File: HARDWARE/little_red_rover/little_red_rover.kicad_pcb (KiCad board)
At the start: 2 copper layers, 127.3 x 82.2 mm, 38 parts, among them J1 USB_C_Receptacle_USB2.0_14P, J2 Conn_01x04_Socket, J3 Conn_01x02_Socket, J4 Conn_01x02_Socket, U1 ESP32-C3-MINI-1, U2 BQ24230RGT, U3 MIC5504-3.3YM5, U4 MIC2876-5.0YMT-TR, U5 DRV8212P, U6 DRV8212P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

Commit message: v1.0 board layout
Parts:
- added R14: 10k, Capacitor_SMD:C_0603_1608Metric_Pad1.08x0.95mm_HandSolder, F.Cu at (190.0, 104.4)
- added R15: 10k, Capacitor_SMD:C_0603_1608Metric_Pad1.08x0.95mm_HandSolder, F.Cu at (190.0, 106.0)
- added U9: LSM6DS3, Package_LGA:LGA-14_3x2.5mm_P0.5mm_LayoutBorder3x4y, F.Cu at (190.0, 110.0)
- J1: footprint Connector_USB:USB_C_Receptacle_GCT_USB4135-GF-A_6P_TopMnt_Horizontal -> Connector_USB:USB_C_Receptacle_GCT_USB4105-xx-A_16P_TopMnt_Horizontal
- moved R12 131.9 mm to (195.5, 112.5)
- moved R10 130.7 mm to (203.6, 92.0), turned to 180 degrees
- moved R5 121.8 mm to (154.9, 134.8), turned to 180 degrees
- moved R4 121.6 mm to (150.9, 134.8)
- moved R11 120.4 mm to (194.1, 90.5)
- moved R2 119.9 mm to (144.7, 131.6)
- moved R9 107.5 mm to (119.4, 131.2), turned to -90 degrees
- moved R1 107.5 mm to (140.8, 131.7), turned to 180 degrees
- moved C6 102.0 mm to (119.4, 134.7), turned to -90 degrees
- moved C4 97.9 mm to (117.4, 126.1)
- moved R3 95.7 mm to (108.5, 123.3), turned to 90 degrees
- moved C3 94.3 mm to (116.4, 120.1), turned to 180 degrees
- moved C1 94.0 mm to (106.5, 118.3), turned to 90 degrees
- moved C5 90.5 mm to (110.5, 123.3), turned to -90 degrees
- moved C2 89.1 mm to (110.5, 114.3), turned to 90 degrees
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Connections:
- C1 pad 1: +5V -> /usb_5v
- J1 pad A9: +5V -> /usb_5v
- J1 pad B9: +5V -> /usb_5v
- U1 pad 5: unconnected-(U1-GPIO2/ADC1_CH2-Pad5) -> /imu_scl
- U1 pad 6: unconnected-(U1-GPIO3/ADC1_CH3-Pad6) -> /imu_sda
- U2 pad 13: +5V -> /usb_5v
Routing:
- net +3.3V: track 0.00 -> 251.1 mm, vias 0 -> 2
- net +5V: track 0.00 -> 217.3 mm, vias 0 -> 5
- net /motor_sleep: track 0.00 -> 106.0 mm, vias 0 -> 3
- net /lidar_tx: track 0.00 -> 98.8 mm, vias 0 -> 2
- net /charger_out: track 0.00 -> 91.8 mm, vias 0 -> 2
- net Net-(D2-K): track 0.00 -> 89.3 mm
- net /usb_data_+: track 0.00 -> 81.9 mm, vias 0 -> 2
- net Net-(D1-K): track 0.00 -> 80.1 mm
- net /usb_data_-: track 0.00 -> 77.5 mm, vias 0 -> 2
- net /usb_5v: track 0.00 -> 72.5 mm
- net /left_motor_pwm_b: track 0.00 -> 55.9 mm, vias 0 -> 2
- net /left_motor_pwm_a: track 0.00 -> 54.6 mm, vias 0 -> 2
- net /right_motor_pwm_b: track 0.00 -> 52.2 mm, vias 0 -> 2
- net Net-(BT1-+): track 0.00 -> 52.1 mm, vias 0 -> 3
- net /right_motor_pwm_a: track 0.00 -> 46.9 mm
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- added copper zone on B.Cu, net GND
- added copper zone on F.Cu, net GND
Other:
- board text added: "little red rover v1.0"

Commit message: Update pcb outline, add threaded inserts
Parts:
- added C10: 0.1uF, Capacitor_SMD:C_0603_1608Metric_Pad1.08x0.95mm_HandSolder, F.Cu at (162.0, 86.8)
- added C7: 10uF, Capacitor_SMD:C_0603_1608Metric_Pad1.08x0.95mm_HandSolder, F.Cu at (156.2, 110.0)
- added C8: 10uF, Capacitor_SMD:C_0603_1608Metric_Pad1.08x0.95mm_HandSolder, F.Cu at (159.6, 85.8)
- added C9: 0.1uF, Capacitor_SMD:C_0603_1608Metric_Pad1.08x0.95mm_HandSolder, F.Cu at (159.4, 113.0)
- added REF**: m3_threaded_insert, digikey_imports:m3_threaded_insert, F.Cu at (163.5, 81.9)
- added REF**: m3_threaded_insert, digikey_imports:m3_threaded_insert, F.Cu at (163.5, 117.9)
- added REF**: m3_threaded_insert, digikey_imports:m3_threaded_insert, F.Cu at (92.2, 99.9)
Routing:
- net +3.3V: track 251.1 -> 260.8 mm, vias 2 -> 4
- net /left_motor_pwm_b: track 55.9 -> 55.0 mm
- net +5V: track 217.3 -> 217.6 mm, vias 5 -> 7
- net GND: vias 23 -> 28
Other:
- outline, holes or cut-outs redrawn

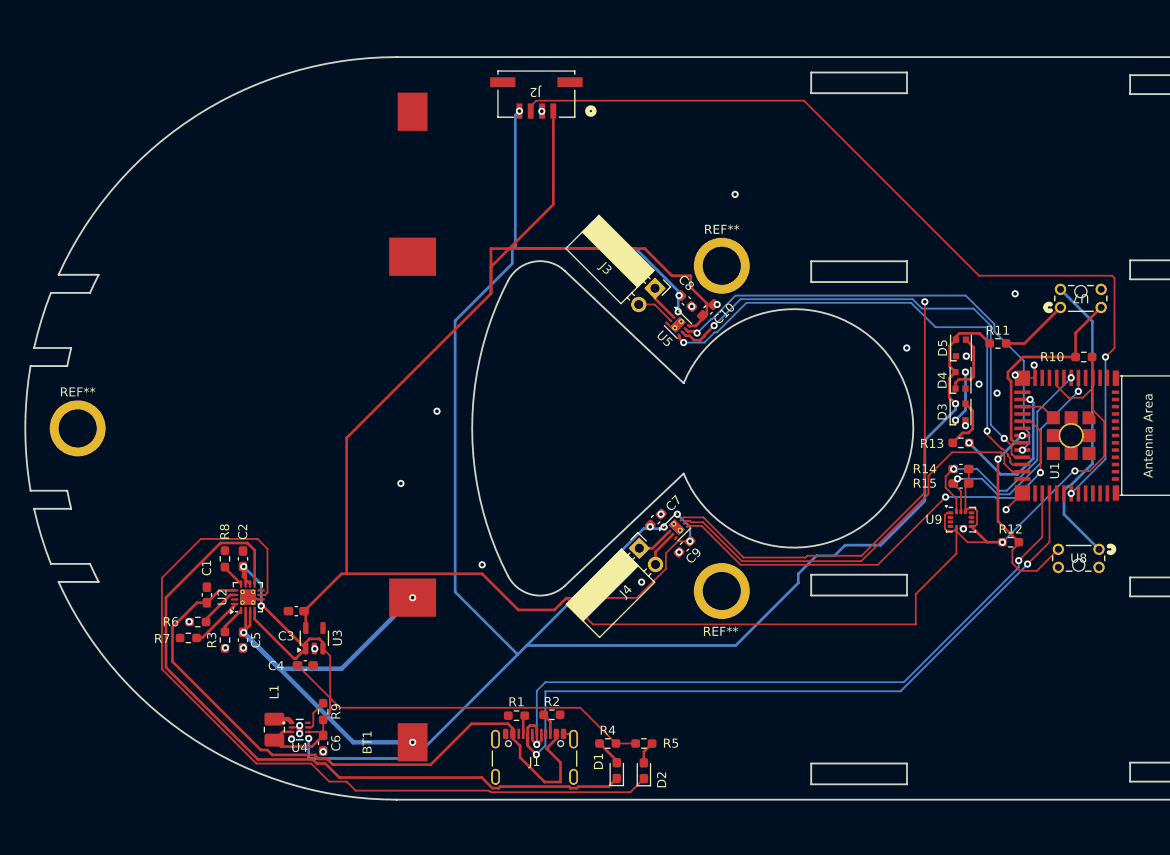
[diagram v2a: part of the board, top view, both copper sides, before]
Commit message: Layout fixes + added QR code
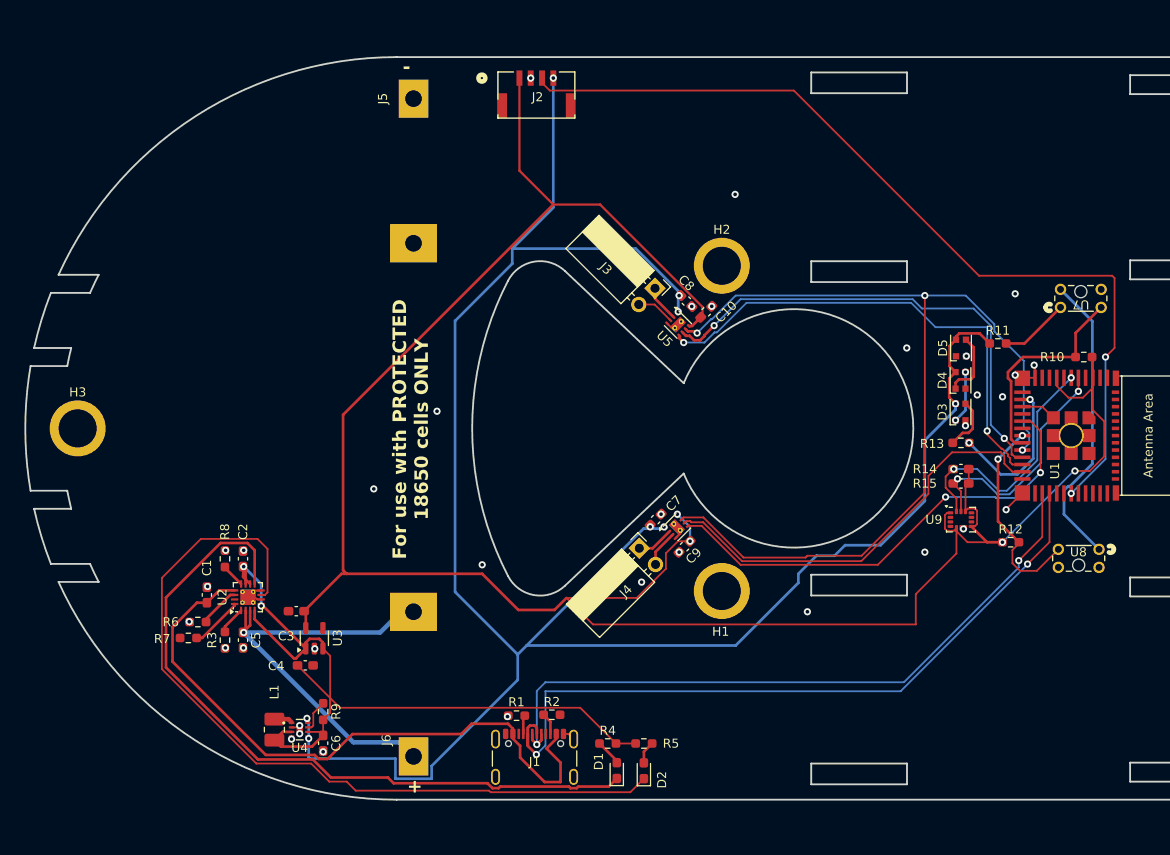
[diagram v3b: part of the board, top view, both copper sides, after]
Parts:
- removed BT1: Battery_Cell, digikey_imports:18650_holder
- added G***: LOGO, digikey_imports:qr_code, B.Cu at (196.2, 127.8)
- added J5: Conn_01x01_Socket, digikey_imports:18650_holder, F.Cu at (129.4, 63.4)
- added J6: Conn_01x01_Socket, digikey_imports:18650_holder, F.Cu at (129.4, 136.2)
- H1, H2, H3: renamed from REF**; value m3_threaded_insert -> MountingHole
- moved C10 0.28 mm to (161.8, 87.0)
- moved J2 0.10 mm to (143.0, 63.0), turned to 0 degrees
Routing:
- net +5V: track 217.6 -> 231.3 mm, vias 7 -> 8
- net +3.3V: track 260.8 -> 254.3 mm
- net Net-(J6-Pin_1): track 52.1 -> 49.0 mm, vias 3 -> 1
- net GND: track 16.5 -> 17.4 mm, vias 28 -> 34
- net /motor_sleep: track 106.2 -> 106.9 mm
- net /usb_5v: track 72.5 -> 71.9 mm
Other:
- board text added: "+"
- board text added: "-"
- board text added: "For use with PROTECTED 18650 cells ONLY"

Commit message: Add hardware README
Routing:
- net GND: track 17.4 -> 19.6 mm

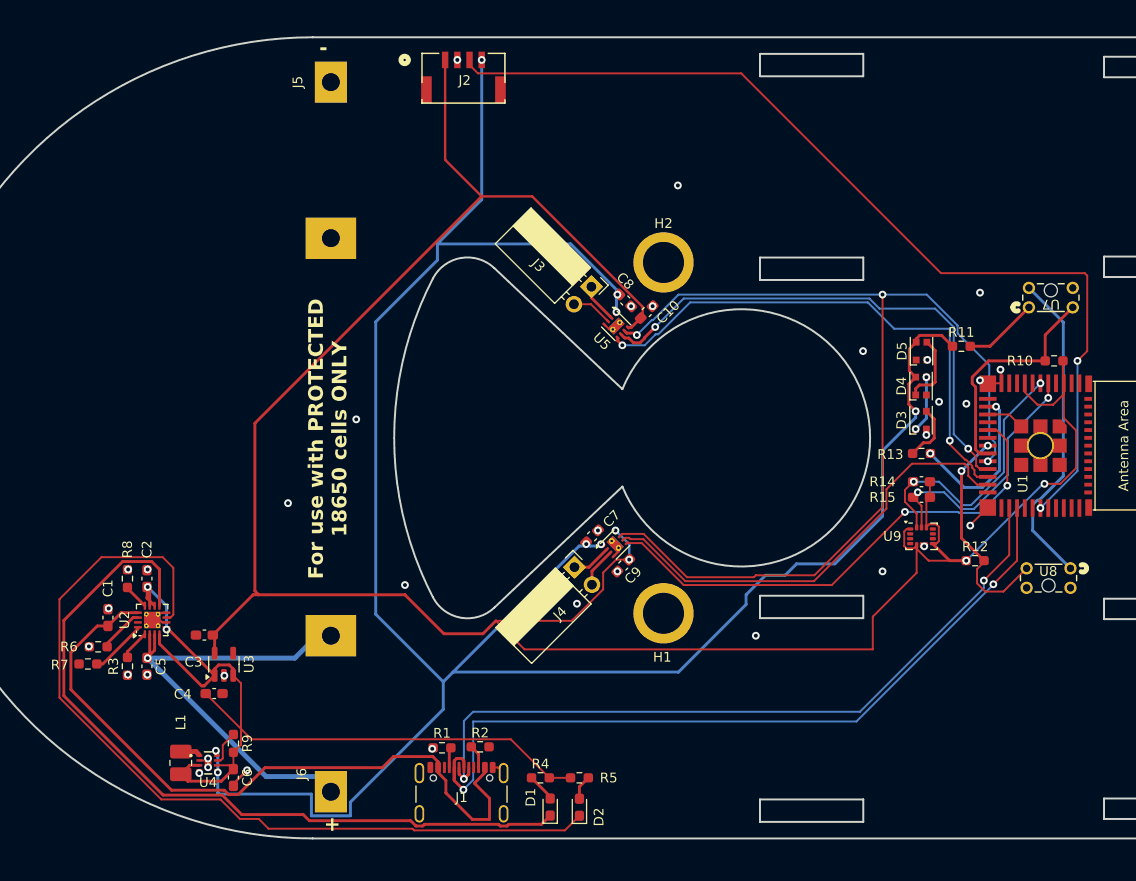
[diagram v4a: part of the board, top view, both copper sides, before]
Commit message: Change 5v boost converter due to shortage
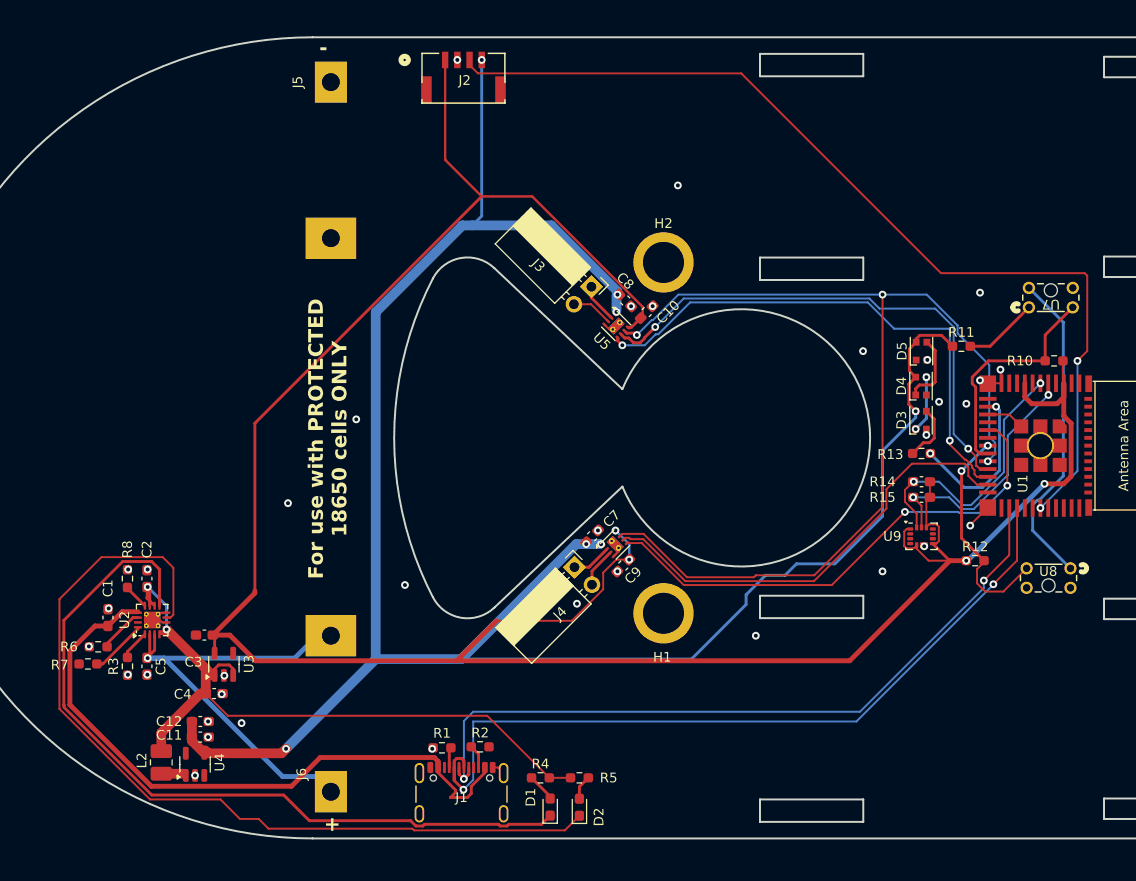
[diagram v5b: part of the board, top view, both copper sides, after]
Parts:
- removed C6: 4.7uF, Capacitor_SMD:C_0603_1608Metric_Pad1.08x0.95mm_HandSolder
- removed L1: 1uH, Inductor_SMD:L_1008_2520Metric_Pad1.43x2.20mm_HandSolder
- removed R9: 1M, Resistor_SMD:R_0603_1608Metric_Pad0.98x0.95mm_HandSolder
- added C11: 10uF, Capacitor_SMD:C_0603_1608Metric_Pad1.08x0.95mm_HandSolder, F.Cu at (116.0, 130.6)
- added C12: 10uF, Capacitor_SMD:C_0603_1608Metric_Pad1.08x0.95mm_HandSolder, F.Cu at (116.0, 129.0)
- added L2: 1uH, Inductor_SMD:L_1008_2520Metric_Pad1.43x2.20mm_HandSolder, F.Cu at (112.0, 133.2)
- U4: value MIC2876-5.0YMT-TR -> TPS613222ADBV; footprint digikey_imports:UDFN8_2X2_MCH-L -> Package_TO_SOT_SMD:SOT-23-5
- moved U4 1.35 mm to (115.5, 133.4), turned to 90 degrees
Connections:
- U4 pad 3: /charger_out -> unconnected-(U4-NC-Pad3)
- U4 pad 4: GND -> +5V
- U4 pad 5: +5V -> unconnected-(U4-NC-Pad5)
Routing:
- net /charger_out: track 91.7 -> 72.1 mm
- net +5V: track 231.3 -> 215.6 mm, vias 8 -> 7
- net +3.3V: track 254.3 -> 263.4 mm
- net /usb_5v: track 71.9 -> 67.0 mm
- net Net-(U4-/PG): track 3.60 -> 0.00 mm
- net GND: track 19.6 -> 16.4 mm, vias 34 -> 35
- net Net-(D1-K): track 80.1 -> 80.8 mm
- net Net-(D2-K): track 89.3 -> 90.0 mm
